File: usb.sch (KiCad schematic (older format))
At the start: 35 parts, among them IC1 OSD335x, IC2 SN74LVC2G241DCUR, U5 TPS2065CDGN, U6 TPD4S012, U7 TPD4S012

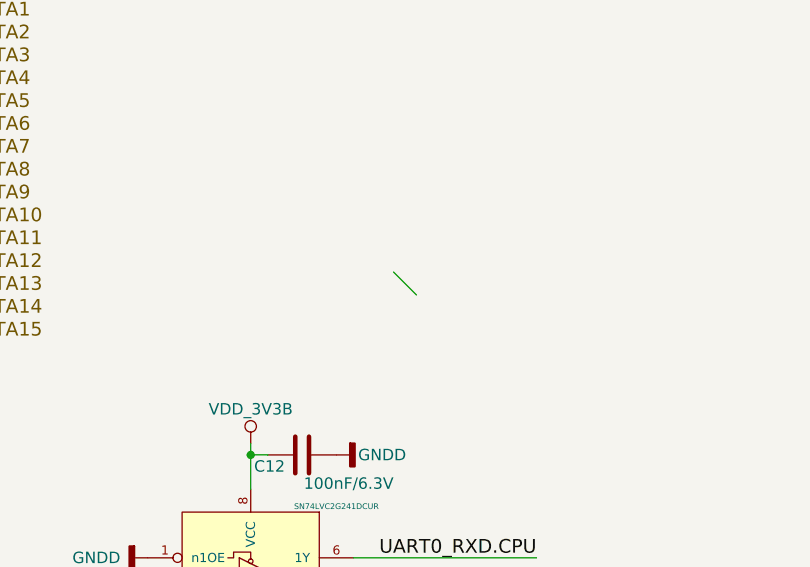
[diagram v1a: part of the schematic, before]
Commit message: add clamping protection for 3v3a and 3v3b
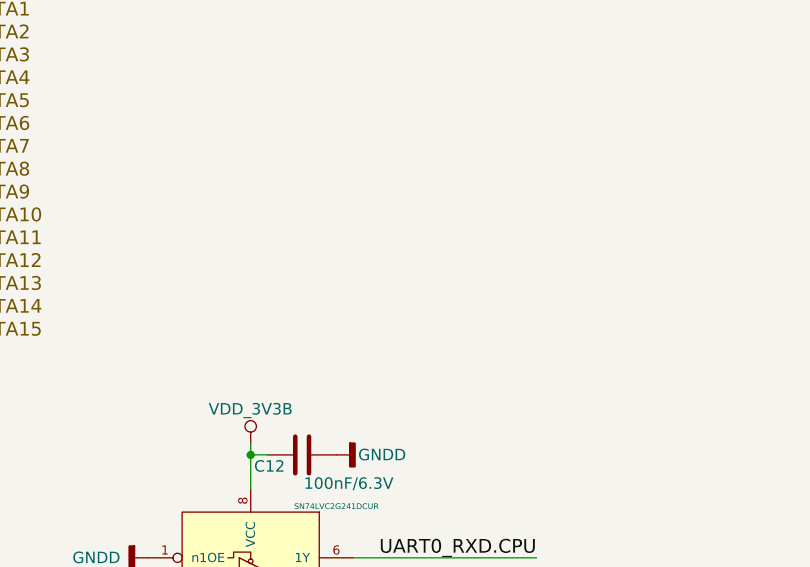
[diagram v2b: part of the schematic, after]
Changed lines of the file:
@@
 $EndComp
 $Comp
-L USB_DC #PWR070
+L USB_DC #PWR073
 U 1 1 58ACAA5E
 P 5550 5850
-F 0 "#PWR070" H 5550 5700 50  0001 C CNN
+F 0 "#PWR073" H 5550 5700 50  0001 C CNN
 F 1 "USB_DC" V 5550 6100 50  0000 C CNN
 F 2 "" H 5550 5850 50  0000 C CNN
@@
 $EndComp
 $Comp
-L GNDD #PWR071
+L GNDD #PWR074
 U 1 1 58ACAB63
 P 6050 6775
-F 0 "#PWR071" H 6050 6525 50  0001 C CNN
+F 0 "#PWR074" H 6050 6525 50  0001 C CNN
 F 1 "GNDD" H 6050 6625 50  0000 C CNN
 F 2 "" H 6050 6775 50  0000 C CNN
@@
 $EndComp
 $Comp
-L USB_DC #PWR072
+L USB_DC #PWR075
 U 1 1 58ACAD7C
 P 5625 4900
-F 0 "#PWR072" H 5625 4750 50  0001 C CNN
+F 0 "#PWR075" H 5625 4750 50  0001 C CNN
 F 1 "USB_DC" V 5625 5150 50  0000 C CNN
 F 2 "" H 5625 4900 50  0000 C CNN
@@
 $EndComp
 $Comp
-L GNDD #PWR073
+L GNDD #PWR076
 U 1 1 58ACB114
 P 4750 6775
-F 0 "#PWR073" H 4750 6525 50  0001 C CNN
+F 0 "#PWR076" H 4750 6525 50  0001 C CNN
 F 1 "GNDD" H 4750 6625 50  0000 C CNN
 F 2 "" H 4750 6775 50  0000 C CNN
@@
 $EndComp
 $Comp
-L GNDD #PWR074
+L GNDD #PWR077
 U 1 1 58ACB72B
 P 5625 5600
-F 0 "#PWR074" H 5625 5350 50  0001 C CNN
+F 0 "#PWR077" H 5625 5350 50  0001 C CNN
 F 1 "GNDD" V 5625 5400 50  0000 C CNN
 F 2 "" H 5625 5600 50  0000 C CNN
@@
 $EndComp
 $Comp
-L GNDD #PWR075
+L GNDD #PWR078
 U 1 1 58ACC7E4
 P 3100 7475
-F 0 "#PWR075" H 3100 7225 50  0001 C CNN
+F 0 "#PWR078" H 3100 7225 50  0001 C CNN
 F 1 "GNDD" H 3100 7325 50  0000 C CNN
 F 2 "" H 3100 7475 50  0000 C CNN
@@
 $EndComp
 $Comp
-L GNDD #PWR076
+L GNDD #PWR079
 U 1 1 58ACCD7F
 P 3600 6525
-F 0 "#PWR076" H 3600 6275 50  0001 C CNN
+F 0 "#PWR079" H 3600 6275 50  0001 C CNN
 F 1 "GNDD" H 3600 6375 50  0000 C CNN
 F 2 "" H 3600 6525 50  0000 C CNN
@@
 $EndComp
 $Comp
-L SYS_5V #PWR077
+L SYS_5V #PWR080
 U 1 1 58ACCF48
 P 3600 6075
-F 0 "#PWR077" H 3600 5925 50  0001 C CNN
+F 0 "#PWR080" H 3600 5925 50  0001 C CNN
 F 1 "SYS_5V" H 3600 6225 50  0000 C CNN
 F 2 "" H 3600 6075 50  0000 C CNN
@@
 $EndComp
 $Comp
-L GNDD #PWR078
+L GNDD #PWR081
 U 1 1 58ACD3E3
 P 2650 6925
-F 0 "#PWR078" H 2650 6675 50  0001 C CNN
+F 0 "#PWR081" H 2650 6675 50  0001 C CNN
 F 1 "GNDD" H 2650 6775 50  0000 C CNN
 F 2 "" H 2650 6925 50  0000 C CNN
@@
 $EndComp
 $Comp
-L VDD_3V3A #PWR079
+L VDD_3V3A #PWR082
 U 1 1 58ACD7EC
 P 1850 6075
-F 0 "#PWR079" H 1850 5925 50  0001 C CNN
+F 0 "#PWR082" H 1850 5925 50  0001 C CNN
 F 1 "VDD_3V3A" H 1850 6225 50  0000 C CNN
 F 2 "" H 1850 6075 50  0000 C CNN
@@
 tantalum cap
 $Comp
-L PWR_FLAG #FLG080
+L PWR_FLAG #FLG083
 U 1 1 58C56F63
 P 1200 5375
-F 0 "#FLG080" H 1200 5450 50  0001 C CNN
+F 0 "#FLG083" H 1200 5450 50  0001 C CNN
 F 1 "PWR_FLAG" H 1200 5525 50  0000 C CNN
 F 2 "" H 1200 5375 50  0001 C CNN
@@
 	3675 3300 4475 3300
 $Comp
-L GNDD #PWR081
+L GNDD #PWR084
 U 1 1 58E27E10
 P 3225 3975
-F 0 "#PWR081" H 3225 3725 50  0001 C CNN
+F 0 "#PWR084" H 3225 3725 50  0001 C CNN
 F 1 "GNDD" H 3225 3825 50  0000 C CNN
 F 2 "" H 3225 3975 50  0001 C CNN
@@
 	3225 3975 3225 3900
 $Comp
-L GNDD #PWR082
+L GNDD #PWR085
 U 1 1 58E27E17
 P 2775 3300
-F 0 "#PWR082" H 2775 3050 50  0001 C CNN
+F 0 "#PWR085" H 2775 3050 50  0001 C CNN
 F 1 "GNDD" V 2775 3075 50  0000 C CNN
 F 2 "" H 2775 3300 50  0001 C CNN
@@
 $EndComp
 $Comp
-L VDD_3V3B #PWR083
+L VDD_3V3B #PWR086
 U 1 1 58E27E1D
 P 2775 3500
-F 0 "#PWR083" H 2775 3350 50  0001 C CNN
+F 0 "#PWR086" H 2775 3350 50  0001 C CNN
 F 1 "VDD_3V3B" V 2775 3800 50  0000 C CNN
 F 2 "" H 2775 3500 50  0000 C CNN
@@
 $EndComp
 $Comp
-L GNDD #PWR084
+L GNDD #PWR087
 U 1 1 58E27E2A
 P 3600 2850
-F 0 "#PWR084" H 3600 2600 50  0001 C CNN
+F 0 "#PWR087" H 3600 2600 50  0001 C CNN
 F 1 "GNDD" V 3600 2650 50  0000 C CNN
 F 2 "" H 3600 2850 50  0000 C CNN
@@
 	3225 2800 3225 3000
 $Comp
-L VDD_3V3B #PWR085
+L VDD_3V3B #PWR088
 U 1 1 58E27E32
 P 3225 2800
-F 0 "#PWR085" H 3225 2650 50  0001 C CNN
+F 0 "#PWR088" H 3225 2650 50  0001 C CNN
 F 1 "VDD_3V3B" H 3225 2950 50  0000 C CNN
 F 2 "" H 3225 2800 50  0000 C CNN
@@
 	2125 3400 2775 3400
 $Comp
-L GNDD #PWR086
+L GNDD #PWR089
 U 1 1 58E27E42
 P 2200 4075
-F 0 "#PWR086" H 2200 3825 50  0001 C CNN
+F 0 "#PWR089" H 2200 3825 50  0001 C CNN
 F 1 "GNDD" H 2200 3925 50  0000 C CNN
 F 2 "" H 2200 4075 50  0001 C CNN
@@
 Connection ~ 10400 2400
 $Comp
-L VDD_3V3B #PWR087
+L VDD_3V3B #PWR090
 U 1 1 58D9F757
 P 10600 2350
-F 0 "#PWR087" H 10600 2200 50  0001 C CNN
+F 0 "#PWR090" H 10600 2200 50  0001 C CNN
 F 1 "VDD_3V3B" H 10600 2500 50  0000 C CNN
 F 2 "" H 10600 2350 50  0000 C CNN
@@
 $EndComp
 $Comp
-L GNDD #PWR088
+L GNDD #PWR091
 U 1 1 58D9F75D
 P 9700 5525
-F 0 "#PWR088" H 9700 5275 50  0001 C CNN
+F 0 "#PWR091" H 9700 5275 50  0001 C CNN
 F 1 "GNDD" H 9700 5375 50  0000 C CNN
 F 2 "" H 9700 5525 50  0001 C CNN
@@
 AIN7
 $Comp
-L VDD_ADC #PWR089
+L VDD_ADC #PWR092
 U 1 1 58DA7836
 P 6550 1600
-F 0 "#PWR089" H 6550 1450 50  0001 C CNN
+F 0 "#PWR092" H 6550 1450 50  0001 C CNN
 F 1 "VDD_ADC" V 6550 1875 50  0000 C CNN
 F 2 "" H 6550 1600 50  0000 C CNN
@@
 Connection ~ 6600 1700
 $Comp
-L GNDA #PWR090
+L GNDA #PWR093
 U 1 1 58DA7ECC
 P 6550 1950
-F 0 "#PWR090" H 6550 1700 50  0001 C CNN
+F 0 "#PWR093" H 6550 1700 50  0001 C CNN
 F 1 "GNDA" V 6550 1725 50  0000 C CNN
 F 2 "" H 6550 1950 50  0001 C CNN
@@
 Text HLabel 1700 2300 2    60   BiDi ~ 0
 LCD_DATA15
-Entry Wire Line
-	3850 2050 3950 2150
 $EndSCHEMATC

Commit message: sch updated
Signed-off-by: Pablo Ridolfi <pabloridolfi@outlook.com>
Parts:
- removed C14, C15: 100nF/6.3V, Capacitors_SMD:C_0402, symbol C
- removed U6, U7: TPD4S012, footprints:SON-6, symbol TPD4S012
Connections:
- no-connect marks 10 -> 9
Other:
- moved on the sheet: C13, L2, L3, R6, R8, U5

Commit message: sch updated
Signed-off-by: Pablo Ridolfi <pabloridolfi@outlook.com>
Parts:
- removed IC1: OSD335x, footprints:OSD3358-BAS-BGA400, symbol OSD335x-RESCUE-mateboard
- added IC1: OSD335x, GHI-SoMs-Processors_OSD3358, symbol OSD335x
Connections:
- net AIN0: now also IC1.B6 (AIN0)
- net AIN1: now also IC1.C7 (AIN1)
- net AIN2: now also IC1.B7 (AIN2)
- net AIN3: now also IC1.A7 (AIN3)
- net AIN4: now also IC1.C8 (AIN4)
- net AIN5: now also IC1.B8 (AIN5)
- net AIN6: now also IC1.A8 (AIN6)
- net AIN7: now also IC1.C9 (AIN7)
- net BT_EN.SIP: now also IC1.K17 (MII1_TXD0)
- net BT_HCI_CTS.SIP: now also IC1.M17 (MDIO_DATA)
- net BT_HCI_RTS.SIP: now also IC1.M18 (MDIO_CLK)
- net BT_HCI_RX.SIP: now also IC1.L17 (MII1_RXD3)
- net BT_HCI_TX.SIP: now also IC1.L16 (MII1_RXD2)
- net GNDA: now also IC1.A6 (AGND_1), IC1.A9 (AGND_0)
- net GPIO3_19: now also IC1.C13 (GPIO3_19)
- net GPIO3_21: now also IC1.A14 (GPIO3_21)
- net I2C1_SCL: now also IC1.A16 (I2C1_SCL)
- net I2C1_SDA: now also IC1.B16 (I2C1_SDA)
- net I2C2_SCL: now also IC1.D17 (I2C2_SCL)
- net I2C2_SDA: now also IC1.D18 (I2C2_SDA)
- net LCD_DATA0: now also IC1.R1 (LCD_DATA0)
- net LCD_DATA1: now also IC1.R2 (LCD_DATA1)
- net LCD_DATA10: now also IC1.U3 (LCD_DATA10)
- net LCD_DATA11: now also IC1.U4 (LCD_DATA11)
- net LCD_DATA12: now also IC1.V2 (LCD_DATA12)
- net LCD_DATA13: now also IC1.V3 (LCD_DATA13)
- net LCD_DATA14: now also IC1.V4 (LCD_DATA14)
- net LCD_DATA15: now also IC1.T5 (LCD_DATA15)
- net LCD_DATA2: now also IC1.R3 (LCD_DATA2)
- net LCD_DATA3: now also IC1.R4 (LCD_DATA3)
- net LCD_DATA4: now also IC1.T1 (LCD_DATA4)
- net LCD_DATA5: now also IC1.T2 (LCD_DATA5)
- net LCD_DATA6: now also IC1.T3 (LCD_DATA6)
- net LCD_DATA7: now also IC1.T4 (LCD_DATA7)
- net LCD_DATA8: now also IC1.U1 (LCD_DATA8)
- net LCD_DATA9: now also IC1.U2 (LCD_DATA9)
- net LCD_DE: now also IC1.R6 (LCD_DE)
- net LCD_HSYNC: now also IC1.R5 (LCD_HSYNC)
- net LCD_PCLK: now also IC1.V5 (LCD_PCLK)
- net LCD_VSYNC: now also IC1.U5 (LCD_VSYNC)
- net LS_BUF_OE.SIP: now also IC1.L18 (MII_RXCLK)
- net SPI1_CLK: now also IC1.A13 (SPI1_CLK)
- net SPI1_CS0: now also IC1.C12 (SPI1_CS0)
- net SPI1_D0: now also IC1.B13 (SPI1_D0)
- net SPI1_D1: now also IC1.D12 (SPI1_D1)
- net UART0_RXD.CPU: now also IC1.E15 (UART0_RXD)
- net UART0_TXD.CPU: now also IC1.E16 (UART0_TXD)
- net UART1_RXD: now also IC1.D16 (UART1_RXD)
- net UART1_TXD: now also IC1.D15 (UART1_TXD)
- net UART2_RXD: now also IC1.A17 (UART2_RXD)
- net UART2_TXD: now also IC1.B17 (UART2_TXD)
- net USB0_DM: now also IC1.N18 (USB0_DM)
- net USB0_DP: now also IC1.N17 (USB0_DP)
- net USB0_ID: now also IC1.P16 (USB0_ID)
- net USB1_DM: now also IC1.R18 (USB1_DM)
- net USB1_DP: now also IC1.R17 (USB1_DP)
- net USB1_DRVVBUS: now also IC1.F15 (USB1_DRVVBUS)
- net VDD_ADC: now also IC1.A4 (VDD_ADC_1), IC1.A5 (VDD_ADC_0), IC1.B9 (VREFP_ADC)
- net WL_EN.SIP: now also IC1.K18 (MII1_TXCLK)
- net WL_IRQ.SIP: now also IC1.H18 (MII1_REFCLK)
- net WL_SDIO_CLK.SIP: now also IC1.L15 (MII1_RXD1)
- net WL_SDIO_CMD.SIP: now also IC1.J16 (MII1_TXEN)
- net WL_SDIO_D0.SIP: now also IC1.J17 (MII1_RXDV)
- net WL_SDIO_D1.SIP: now also IC1.J18 (MII1_TXD3)
- net WL_SDIO_D2.SIP: now also IC1.K15 (MII1_TXD2)
- net WL_SDIO_D3.SIP: now also IC1.H16 (MII1_COL)
- net at R9.2: now also IC1.P15 (USB0_VBUS)
- net at R10.2: now also IC1.P17 (USB1_ID)
- net at L3.2: now also IC1.T18 (USB1_VBUS)
- net at R11.2: now also IC1.B12 (GPIO3_18)
- net at R12.2: now also IC1.C18 (GPIO0_7)
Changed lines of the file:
@@
 	1    0    0    1
-$EndComp
-$Comp
-L OSD335x-RESCUE-mateboard IC1
-U 2 1 58DCDABD
-P 7850 3400
-AR Path="/58DCDABD" Ref="IC1"  Part="2"
-AR Path="/58AF1DA5/58DCDABD" Ref="IC1"  Part="2"
-F 0 "IC1" H 7775 3425 45  0000 L BNN
-F 1 "OSD335x" H 7700 3325 45  0000 L BNN
-F 2 "footprints:OSD3358-BAS-BGA400" H 7880 3550 20  0001 C CNN
-F 3 "" H 7850 3400 60  0001 C CNN
-	2    7850 3400
-	1    0    0    -1
 $EndComp
 Wire Wire Line
@@
 Wire Wire Line
 	3550 4400 6650 4400
+$Comp
+L OSD335x IC1
+U 2 1 594BB330
+P 7850 3400
+AR Path="/594BB330" Ref="IC1"  Part="2"
+AR Path="/58AF1DA5/594BB330" Ref="IC1"  Part="2"
+F 0 "IC1" H 7150 6250 45  0000 C CNN
+F 1 "OSD335x" H 7550 6250 45  0000 C CNN
+F 2 "GHI-SoMs-Processors_OSD3358" H 7880 3550 20  0001 C CNN
+F 3 "" H 7850 3400 60  0001 C CNN
+	2    7850 3400
+	1    0    0    -1
+$EndComp
 $EndSCHEMATC

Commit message: footprints updated, add power led
Signed-off-by: Pablo Ridolfi <pabloridolfi@outlook.com>
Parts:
- IC1: footprint GHI-SoMs-Processors_OSD3358 -> footprints:OSD3358-BAS-BGA400
- U5: footprint Housings_SSOP:VSSOP-8_2.3x2mm_Pitch0.5mm -> Housings_SSOP:MSOP-8-1EP_3x3mm_Pitch0.65mm
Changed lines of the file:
@@
 F 0 "U5" H 4875 6650 60  0000 C CNN
 F 1 "TPS2065CDGN" H 5125 6550 60  0000 C CNN
-F 2 "Housings_SSOP:VSSOP-8_2.3x2mm_Pitch0.5mm" H 4800 5950 60  0001 C CNN
+F 2 "Housings_SSOP:MSOP-8-1EP_3x3mm_Pitch0.65mm" H 4800 5950 60  0001 C CNN
 F 3 "" H 4800 5950 60  0001 C CNN
 	1    5050 6275
@@
 F 0 "IC1" H 7150 6250 45  0000 C CNN
 F 1 "OSD335x" H 7550 6250 45  0000 C CNN
-F 2 "GHI-SoMs-Processors_OSD3358" H 7880 3550 20  0001 C CNN
+F 2 "footprints:OSD3358-BAS-BGA400" H 7880 3550 20  0001 C CNN
 F 3 "" H 7850 3400 60  0001 C CNN
 	2    7850 3400

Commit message: mateboard v1.0
Signed-off-by: Pablo Ridolfi <pabloridolfi@outlook.com>
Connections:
- net USB0_DM renamed USB0_D-
- net USB0_DP renamed USB0_D+
- net USB1_DM renamed USB1_D-
- net USB1_DP renamed USB1_D+
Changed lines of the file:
@@
 $EndDescr
 Text HLabel 3550 4400 0    60   BiDi ~ 0
-USB0_DP
+USB0_D+
 Text HLabel 3550 4500 0    60   BiDi ~ 0
-USB0_DM
+USB0_D-
 Text HLabel 3550 4700 0    60   BiDi ~ 0
 USB0_ID
@@
 $EndComp
 Text HLabel 3550 5100 0    60   BiDi ~ 0
-USB1_DP
+USB1_D+
 Text HLabel 3550 5200 0    60   BiDi ~ 0
-USB1_DM
+USB1_D-
 $Comp
 L TPS2065CDGN U5

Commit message: gerbers updated, bom using kicost
Signed-off-by: Pablo Ridolfi <pabloridolfi@outlook.com>
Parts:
- C13: manf# (none) -> TAJD227M010RNJ
- IC2: manf# (none) -> SN74LVC2G241DCUR
- L2: manf# (none) -> LI0805H151R-10
- L3: manf# (none) -> 73L3R10J
- R10, R12: manf# (none) -> RC0402JR-070RL
- R13: manf# (none) -> RC0402FR-07100KL
- R29: manf# (none) -> RC0402FR-07100RL
- U5: manf# (none) -> TPS2065CDGNR
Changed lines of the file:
@@
 $EndComp
 $Comp
-L USB_DC #PWR80
+L USB_DC #PWR080
 U 1 1 58ACAD7C
 P 5625 4900
-F 0 "#PWR80" H 5625 4750 50  0001 C CNN
+F 0 "#PWR080" H 5625 4750 50  0001 C CNN
 F 1 "USB_DC" V 5625 5150 50  0000 C CNN
 F 2 "" H 5625 4900 50  0000 C CNN
@@
 F 2 "Resistors_SMD:R_0402" V 5705 5600 50  0001 C CNN
 F 3 "" H 5775 5600 50  0000 C CNN
+F 4 "RC0402JR-070RL" V 5775 5600 60  0001 C CNN "manf#"
 	1    5775 5600
 	0    -1   1    0
 $EndComp
 $Comp
-L GNDD #PWR81
+L GNDD #PWR081
 U 1 1 58ACB72B
 P 5625 5600
-F 0 "#PWR81" H 5625 5350 50  0001 C CNN
+F 0 "#PWR081" H 5625 5350 50  0001 C CNN
 F 1 "GNDD" V 5625 5400 50  0000 C CNN
 F 2 "" H 5625 5600 50  0000 C CNN
@@
 F 2 "Housings_SSOP:MSOP-8-1EP_3x3mm_Pitch0.65mm" H 4800 5950 60  0001 C CNN
 F 3 "" H 4800 5950 60  0001 C CNN
+F 4 "TPS2065CDGNR" H 5050 6275 60  0001 C CNN "manf#"
 	1    5050 6275
 	-1   0    0    -1
@@
 F 2 "Resistors_SMD:R_0805" H 5750 5300 50  0001 C CNN
 F 3 "" H 5750 5300 50  0000 C CNN
+F 4 "73L3R10J" V 5750 5300 60  0001 C CNN "manf#"
 	1    5750 5300
 	0    -1   1    0
@@
 F 2 "Resistors_SMD:R_0805" H 4050 5300 50  0001 C CNN
 F 3 "" H 4050 5300 50  0000 C CNN
+F 4 "LI0805H151R-10" V 4050 5300 60  0001 C CNN "manf#"
 	1    4050 5300
 	0    -1   1    0
@@
 $EndComp
 $Comp
-L GNDD #PWR79
+L GNDD #PWR079
 U 1 1 58ACC7E4
 P 5500 7475
-F 0 "#PWR79" H 5500 7225 50  0001 C CNN
+F 0 "#PWR079" H 5500 7225 50  0001 C CNN
 F 1 "GNDD" H 5500 7325 50  0000 C CNN
 F 2 "" H 5500 7475 50  0000 C CNN
@@
 F 2 "Capacitors_Tantalum_SMD:CP_Tantalum_Case-A_EIA-3216-18_Reflow" H 6038 6225 50  0001 C CNN
 F 3 "" H 6000 6375 50  0000 C CNN
+F 4 "TAJD227M010RNJ" H 6000 6375 60  0001 C CNN "manf#"
 	1    6000 6375
 	-1   0    0    -1
 $EndComp
 $Comp
-L GNDD #PWR83
+L GNDD #PWR083
 U 1 1 58ACCD7F
 P 6000 6525
-F 0 "#PWR83" H 6000 6275 50  0001 C CNN
+F 0 "#PWR083" H 6000 6275 50  0001 C CNN
 F 1 "GNDD" H 6000 6375 50  0000 C CNN
 F 2 "" H 6000 6525 50  0000 C CNN
@@
 $EndComp
 $Comp
-L SYS_5V #PWR82
+L SYS_5V #PWR082
 U 1 1 58ACCF48
 P 6000 6075
-F 0 "#PWR82" H 6000 5925 50  0001 C CNN
+F 0 "#PWR082" H 6000 5925 50  0001 C CNN
 F 1 "SYS_5V" H 6000 6225 50  0000 C CNN
 F 2 "" H 6000 6075 50  0000 C CNN
@@
 $EndComp
 $Comp
-L GNDD #PWR78
+L GNDD #PWR078
 U 1 1 58ACD3E3
 P 5050 6925
-F 0 "#PWR78" H 5050 6675 50  0001 C CNN
+F 0 "#PWR078" H 5050 6675 50  0001 C CNN
 F 1 "GNDD" H 5050 6775 50  0000 C CNN
 F 2 "" H 5050 6925 50  0000 C CNN
@@
 $EndComp
 $Comp
-L VDD_3V3A #PWR77
+L VDD_3V3A #PWR077
 U 1 1 58ACD7EC
 P 4250 6075
-F 0 "#PWR77" H 4250 5925 50  0001 C CNN
+F 0 "#PWR077" H 4250 5925 50  0001 C CNN
 F 1 "VDD_3V3A" H 4250 6225 50  0000 C CNN
 F 2 "" H 4250 6075 50  0000 C CNN
@@
 tantalum cap
 $Comp
-L PWR_FLAG #FLG4
+L PWR_FLAG #FLG04
 U 1 1 58C56F63
 P 3600 5375
-F 0 "#FLG4" H 3600 5450 50  0001 C CNN
+F 0 "#FLG04" H 3600 5450 50  0001 C CNN
 F 1 "PWR_FLAG" H 3600 5525 50  0000 C CNN
 F 2 "" H 3600 5375 50  0001 C CNN
@@
 F 2 "Housings_SSOP:VSSOP-8_2.3x2mm_Pitch0.5mm" H 3225 3450 60  0001 C CNN
 F 3 "" H 3225 3450 60  0001 C CNN
+F 4 "SN74LVC2G241DCUR" H 3225 3450 60  0001 C CNN "manf#"
 	1    3225 3450
 	1    0    0    -1
@@
 	3675 3300 4475 3300
 $Comp
-L GNDD #PWR75
+L GNDD #PWR075
 U 1 1 58E27E10
 P 3225 3975
-F 0 "#PWR75" H 3225 3725 50  0001 C CNN
+F 0 "#PWR075" H 3225 3725 50  0001 C CNN
 F 1 "GNDD" H 3225 3825 50  0000 C CNN
 F 2 "" H 3225 3975 50  0001 C CNN
@@
 	3225 3975 3225 3900
 $Comp
-L GNDD #PWR72
+L GNDD #PWR072
 U 1 1 58E27E17
 P 2775 3300
-F 0 "#PWR72" H 2775 3050 50  0001 C CNN
+F 0 "#PWR072" H 2775 3050 50  0001 C CNN
 F 1 "GNDD" V 2775 3075 50  0000 C CNN
 F 2 "" H 2775 3300 50  0001 C CNN
@@
 $EndComp
 $Comp
-L VDD_3V3B #PWR73
+L VDD_3V3B #PWR073
 U 1 1 58E27E1D
 P 2775 3500
-F 0 "#PWR73" H 2775 3350 50  0001 C CNN
+F 0 "#PWR073" H 2775 3350 50  0001 C CNN
 F 1 "VDD_3V3B" V 2775 3800 50  0000 C CNN
 F 2 "" H 2775 3500 50  0000 C CNN
@@
 $EndComp
 $Comp
-L GNDD #PWR76
+L GNDD #PWR076
 U 1 1 58E27E2A
 P 3600 2850
-F 0 "#PWR76" H 3600 2600 50  0001 C CNN
+F 0 "#PWR076" H 3600 2600 50  0001 C CNN
 F 1 "GNDD" V 3600 2650 50  0000 C CNN
 F 2 "" H 3600 2850 50  0000 C CNN
@@
 	3225 2800 3225 3000
 $Comp
-L VDD_3V3B #PWR74
+L VDD_3V3B #PWR074
 U 1 1 58E27E32
 P 3225 2800
-F 0 "#PWR74" H 3225 2650 50  0001 C CNN
+F 0 "#PWR074" H 3225 2650 50  0001 C CNN
 F 1 "VDD_3V3B" H 3225 2950 50  0000 C CNN
 F 2 "" H 3225 2800 50  0000 C CNN
@@
 	2125 3400 2775 3400
 $Comp
-L GNDD #PWR71
+L GNDD #PWR071
 U 1 1 58E27E42
 P 2200 4075
-F 0 "#PWR71" H 2200 3825 50  0001 C CNN
+F 0 "#PWR071" H 2200 3825 50  0001 C CNN
 F 1 "GNDD" H 2200 3925 50  0000 C CNN
 F 2 "" H 2200 4075 50  0001 C CNN
@@
 F 2 "Resistors_SMD:R_0402" V 9630 5200 50  0001 C CNN
 F 3 "" H 9700 5200 50  0001 C CNN
+F 4 "RC0402FR-07100KL" V 9700 5200 60  0001 C CNN "manf#"
 	1    9700 5200
 	1    0    0    -1
@@
 Connection ~ 10400 2400
 $Comp
-L VDD_3V3B #PWR87
+L VDD_3V3B #PWR087
 U 1 1 58D9F757
 P 10600 2350
-F 0 "#PWR87" H 10600 2200 50  0001 C CNN
+F 0 "#PWR087" H 10600 2200 50  0001 C CNN
 F 1 "VDD_3V3B" H 10600 2500 50  0000 C CNN
 F 2 "" H 10600 2350 50  0000 C CNN
@@
 $EndComp
 $Comp
-L GNDD #PWR86
+L GNDD #PWR086
 U 1 1 58D9F75D
 P 9700 5525
-F 0 "#PWR86" H 9700 5275 50  0001 C CNN
+F 0 "#PWR086" H 9700 5275 50  0001 C CNN
 F 1 "GNDD" H 9700 5375 50  0000 C CNN
 F 2 "" H 9700 5525 50  0001 C CNN
@@
 F 2 "Resistors_SMD:R_0402" V 10830 3100 50  0001 C CNN
 F 3 "" H 10900 3100 50  0001 C CNN
+F 4 "RC0402FR-07100RL" V 10900 3100 60  0001 C CNN "manf#"
 	1    10900 3100
 	0    1    1    0
@@
 F 2 "Resistors_SMD:R_0402" V 9430 6000 50  0001 C CNN
 F 3 "" H 9500 6000 50  0001 C CNN
+F 4 "RC0402JR-070RL" V 9500 6000 60  0001 C CNN "manf#"
 	1    9500 6000
 	0    1    1    0
@@
 AIN7
 $Comp
-L VDD_ADC #PWR84
+L VDD_ADC #PWR084
 U 1 1 58DA7836
 P 6550 1600
-F 0 "#PWR84" H 6550 1450 50  0001 C CNN
+F 0 "#PWR084" H 6550 1450 50  0001 C CNN
 F 1 "VDD_ADC" V 6550 1875 50  0000 C CNN
 F 2 "" H 6550 1600 50  0000 C CNN
@@
 Connection ~ 6600 1700
 $Comp
-L GNDA #PWR85
+L GNDA #PWR085
 U 1 1 58DA7ECC
 P 6550 1950
-F 0 "#PWR85" H 6550 1700 50  0001 C CNN
+F 0 "#PWR085" H 6550 1700 50  0001 C CNN
 F 1 "GNDA" V 6550 1725 50  0000 C CNN
 F 2 "" H 6550 1950 50  0001 C CNN
